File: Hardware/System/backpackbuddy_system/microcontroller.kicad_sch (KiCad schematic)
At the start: 10 parts, among them SW2 MCU RESET, U1 ATmega32U4-A, Y1 16MHz

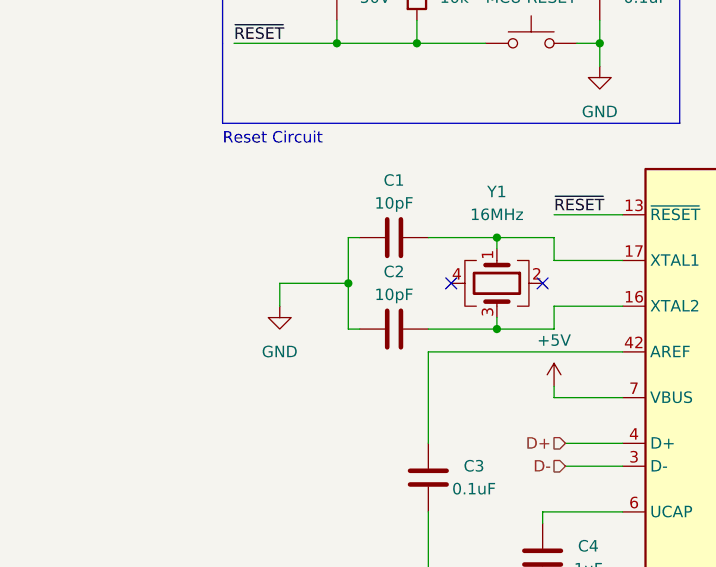
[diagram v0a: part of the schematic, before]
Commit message: fixed table values
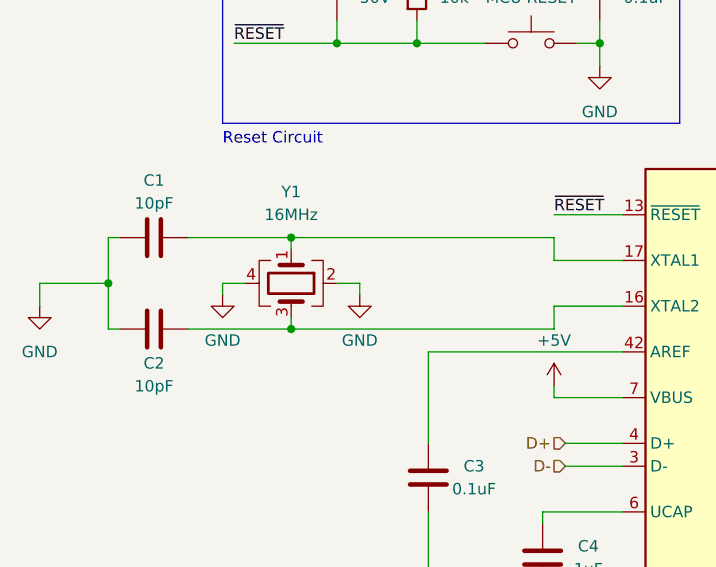
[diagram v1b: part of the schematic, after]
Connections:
- net GND: now also Y1.2, Y1.4
- no-connect marks 11 -> 9
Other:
- moved on the sheet: C1, C2, Y1

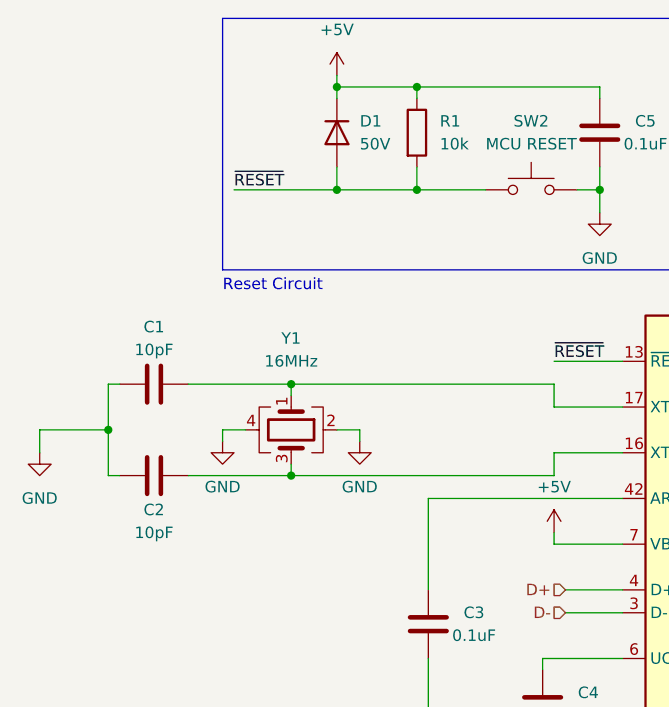
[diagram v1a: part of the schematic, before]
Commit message: changed D1, the MCU reset switch diode from 50V to 1V, changed crystal caps to 22pF
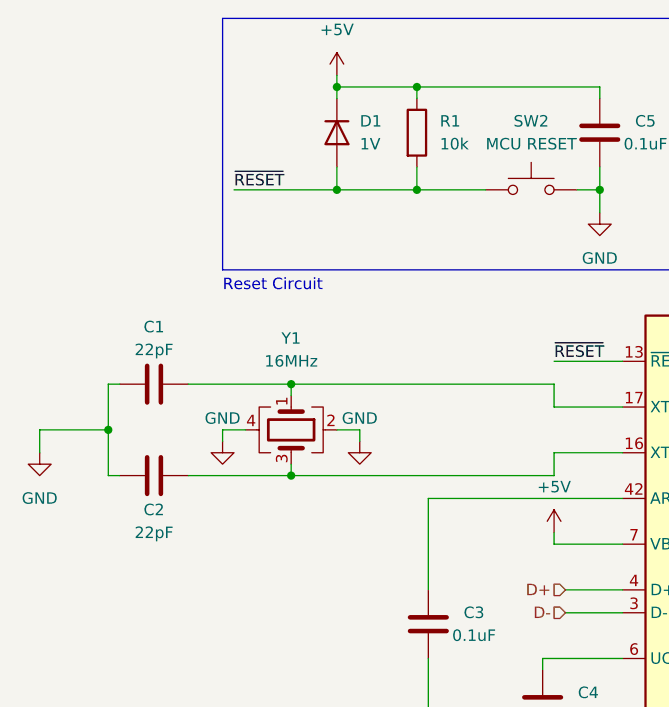
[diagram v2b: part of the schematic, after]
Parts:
- C1, C2: value 10pF -> 22pF
- D1: value 50V -> 1V; MPN DIODE SCHOTTKY 50V 1A SMB -> DIODE RECTIFIER 1V 2A SMB; Stock https://www.digikey.com/en/products/detail/diodes-incorpora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 -> https://www.digikey.com/en/products/detail/micro-commercial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
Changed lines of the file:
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@@
       (effects (font (size 1.27 1.27)) (justify left))
     )
-    (property "Value" "50V" (id 1) (at 102.87 46.9899 90)
+    (property "Value" "1V" (id 1) (at 102.87 46.9899 90)
       (effects (font (size 1.27 1.27)) (justify left))
     )
@@
       (effects (font (size 1.27 1.27)) hide)
     )
-    (property "Datasheet" "~" (id 3) (at 100.33 45.72 0)
-      (effects (font (size 1.27 1.27)) hide)
-    )
-    (property "MPN" "DIODE SCHOTTKY 50V 1A SMB" (id 4) (at 100.33 45.72 0)
-      (effects (font (size 1.27 1.27)) hide)
-    )
-    (property "Stock" "https://www.digikey.com/en/products/detail/diodes-incorporated/B150B-13-F/775856?utm_adgroup=General&utm_source=google&utm_medium=cpc&utm_campaign=PMax%20Shopping_Product_Zombie%20SKUs&utm_term=&utm_content=General" (id 5) (at 100.33 45.72 0)
+    (property "Datasheet" "https://www.mccsemi.com/pdf/Products/US2A-US2M(DO-214AA).pdf" (id 3) (at 100.33 45.72 0)
+      (effects (font (size 1.27 1.27)) hide)
+    )
+    (property "MPN" "DIODE RECTIFIER 1V 2A SMB" (id 4) (at 100.33 45.72 0)
+      (effects (font (size 1.27 1.27)) hide)
+    )
+    (property "Stock" "https://www.digikey.com/en/products/detail/micro-commercial-co/US2D-TP/4936172" (id 5) (at 100.33 45.72 0)
       (effects (font (size 1.27 1.27)) hide)
     )
@@
   )
   (symbol (lib_id "power:GND") (at 87.63 80.01 0) (unit 1)
-    (in_bom yes) (on_board yes) (fields_autoplaced)
+    (in_bom yes) (on_board yes)
     (property "Reference" "#PWR0108" (id 0) (at 87.63 86.36 0)
       (effects (font (size 1.27 1.27)) hide)
     )
-    (property "Value" "GND" (id 1) (at 87.63 85.09 0))
+    (property "Value" "GND" (id 1) (at 87.63 77.47 0))
     (property "Footprint" "" (id 2) (at 87.63 80.01 0)
       (effects (font (size 1.27 1.27)) hide)
@@
   )
   (symbol (lib_id "power:GND") (at 102.87 80.01 0) (unit 1)
-    (in_bom yes) (on_board yes) (fields_autoplaced)
+    (in_bom yes) (on_board yes)
     (property "Reference" "#PWR0107" (id 0) (at 102.87 86.36 0)
       (effects (font (size 1.27 1.27)) hide)
     )
-    (property "Value" "GND" (id 1) (at 102.87 85.09 0))
+    (property "Value" "GND" (id 1) (at 102.87 77.47 0))
     (property "Footprint" "" (id 2) (at 102.87 80.01 0)
       (effects (font (size 1.27 1.27)) hide)
@@
     (in_bom yes) (on_board yes)
     (property "Reference" "C2" (id 0) (at 80.01 87.63 90))
-    (property "Value" "10pF" (id 1) (at 80.01 90.17 90))
+    (property "Value" "22pF" (id 1) (at 80.01 90.17 90))
     (property "Footprint" "Capacitor_SMD:C_0805_2012Metric_Pad1.18x1.45mm_HandSolder" (id 2) (at 83.82 82.8548 0)
       (effects (font (size 1.27 1.27)) hide)
@@
     (in_bom yes) (on_board yes)
     (property "Reference" "C1" (id 0) (at 80.01 67.31 90))
-    (property "Value" "10pF" (id 1) (at 80.01 69.85 90))
+    (property "Value" "22pF" (id 1) (at 80.01 69.85 90))
     (property "Footprint" "Capacitor_SMD:C_0805_2012Metric_Pad1.18x1.45mm_HandSolder" (id 2) (at 83.82 72.6948 0)
       (effects (font (size 1.27 1.27)) hide)

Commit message: decoupling caps
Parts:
- added C20, C21, C22: 10uF, Capacitor_SMD:C_0805_2012Metric_Pad1.18x1.45mm_HandSolder, symbol Device:C
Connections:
- net +5V: now also C20.1, C21.1, C22.1
- net GND: now also C20.2, C21.2, C22.2
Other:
- note added: "MCU DECOUPLING CAPS"
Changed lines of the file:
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@@
   (junction (at 110.49 114.3) (diameter 0) (color 0 0 0 0)
   )
+  (junction (at 185.42 41.91) (diameter 0) (color 0 0 0 0)
+  )
   (junction (at 95.25 83.82) (diameter 0) (color 0 0 0 0)
   )
@@
   (junction (at 144.78 157.48) (diameter 0) (color 0 0 0 0)
   )
+  (junction (at 176.53 41.91) (diameter 0) (color 0 0 0 0)
+  )
+  (junction (at 176.53 54.61) (diameter 0) (color 0 0 0 0)
+  )
   (junction (at 74.93 78.74) (diameter 0) (color 0 0 0 0)
   )
@@
   )
   (junction (at 109.22 40.64) (diameter 0) (color 0 0 0 0)
+  )
+  (junction (at 185.42 54.61) (diameter 0) (color 0 0 0 0)
   )
   (junction (at 100.33 52.07) (diameter 0) (color 0 0 0 0)
@@
     (stroke (width 0) (type default) (color 0 0 0 0))
   )
+  (wire (pts (xy 176.53 52.07) (xy 176.53 54.61))
+    (stroke (width 0) (type default) (color 0 0 0 0))
+  )
   (wire (pts (xy 162.56 78.74) (xy 172.72 78.74))
     (stroke (width 0) (type default) (color 0 0 0 0))
@@
     (stroke (width 0) (type default) (color 0 0 0 0))
   )
+  (wire (pts (xy 185.42 54.61) (xy 194.31 54.61))
+    (stroke (width 0) (type default) (color 0 0 0 0))
+  )
   (wire (pts (xy 162.56 76.2) (xy 172.72 76.2))
     (stroke (width 0) (type default) (color 0 0 0 0))
@@
     (stroke (width 0) (type default) (color 0 0 0 0))
   )
+  (wire (pts (xy 185.42 41.91) (xy 185.42 44.45))
+    (stroke (width 0) (type default) (color 0 0 0 0))
+  )
   (wire (pts (xy 162.56 73.66) (xy 172.72 73.66))
     (stroke (width 0) (type default) (color 0 0 0 0))
@@
     (stroke (width 0) (type default) (color 0 0 0 0))
   )
+  (wire (pts (xy 176.53 41.91) (xy 176.53 44.45))
+    (stroke (width 0) (type default) (color 0 0 0 0))
+  )
   (wire (pts (xy 162.56 71.12) (xy 172.72 71.12))
     (stroke (width 0) (type default) (color 0 0 0 0))
@@
     (stroke (width 0) (type default) (color 0 0 0 0))
   )
+  (wire (pts (xy 176.53 54.61) (xy 185.42 54.61))
+    (stroke (width 0) (type default) (color 0 0 0 0))
+  )
   (wire (pts (xy 162.56 96.52) (xy 172.72 96.52))
     (stroke (width 0) (type default) (color 0 0 0 0))
@@
     (stroke (width 0) (type default) (color 0 0 0 0))
   )
+  (wire (pts (xy 185.42 41.91) (xy 194.31 41.91))
+    (stroke (width 0) (type default) (color 0 0 0 0))
+  )
   (wire (pts (xy 162.56 139.7) (xy 172.72 139.7))
     (stroke (width 0) (type default) (color 0 0 0 0))
@@
     (stroke (width 0) (type default) (color 0 0 0 0))
   )
+  (wire (pts (xy 185.42 52.07) (xy 185.42 54.61))
+    (stroke (width 0) (type default) (color 0 0 0 0))
+  )
+  (wire (pts (xy 194.31 44.45) (xy 194.31 41.91))
+    (stroke (width 0) (type default) (color 0 0 0 0))
+  )
   (polyline (pts (xy 138.43 60.96) (xy 87.63 60.96))
     (stroke (width 0) (type default) (color 0 0 0 0))
@@
     (stroke (width 0) (type default) (color 0 0 0 0))
   )
+  (wire (pts (xy 176.53 40.64) (xy 176.53 41.91))
+    (stroke (width 0) (type default) (color 0 0 0 0))
+  )
   (wire (pts (xy 162.56 104.14) (xy 172.72 104.14))
     (stroke (width 0) (type default) (color 0 0 0 0))
@@
     (stroke (width 0) (type default) (color 0 0 0 0))
   )
+  (wire (pts (xy 176.53 54.61) (xy 176.53 55.88))
+    (stroke (width 0) (type default) (color 0 0 0 0))
+  )
   (wire (pts (xy 125.73 96.52) (xy 132.08 96.52))
     (stroke (width 0) (type default) (color 0 0 0 0))
   )
+  (wire (pts (xy 194.31 52.07) (xy 194.31 54.61))
+    (stroke (width 0) (type default) (color 0 0 0 0))
+  )
   (wire (pts (xy 144.78 63.5) (xy 144.78 58.42))
     (stroke (width 0) (type default) (color 0 0 0 0))
@@
     (stroke (width 0) (type default) (color 0 0 0 0))
   )
+  (wire (pts (xy 176.53 41.91) (xy 185.42 41.91))
+    (stroke (width 0) (type default) (color 0 0 0 0))
+  )
   (wire (pts (xy 162.56 134.62) (xy 172.72 134.62))
     (stroke (width 0) (type default) (color 0 0 0 0))
+  )
+  (text "MCU DECOUPLING CAPS" (at 173.99 33.02 0)
+    (effects (font (size 1.27 1.27)) (justify left bottom))
   )
   (text "Reset Circuit" (at 87.63 63.5 0)
@@
   (hierarchical_label "PF6" (shape bidirectional) (at 172.72 142.24 0)
     (effects (font (size 1.27 1.27)) (justify left))
+  )
+  (symbol (lib_id "Device:C") (at 176.53 48.26 0) (unit 1)
+    (in_bom yes) (on_board yes)
+    (property "Reference" "C20" (id 0) (at 170.18 48.26 0)
+      (effects (font (size 1.27 1.27)) (justify left))
+    )
+    (property "Value" "10uF" (id 1) (at 170.18 50.8 0)
+      (effects (font (size 1.27 1.27)) (justify left))
+    )
+    (property "Footprint" "Capacitor_SMD:C_0805_2012Metric_Pad1.18x1.45mm_HandSolder" (id 2) (at 177.4952 52.07 0)
+      (effects (font (size 1.27 1.27)) hide)
+    )
+    (property "Datasheet" "~" (id 3) (at 176.53 48.26 0)
+      (effects (font (size 1.27 1.27)) hide)
+    )
+    (property "MPN" "CAP CER 10UF 25V X5R 0805" (id 4) (at 176.53 48.26 0)
+      (effects (font (size 1.27 1.27)) hide)
+    )
+    (property "Stock" "https://www.digikey.com/en/products/detail/kyocera-avx/08053D106KAT4A/12153448?utm_adgroup=Capacitors&utm_source=google&utm_medium=cpc&utm_campaign=Shopping_Supplier_AVX%20Corporation&utm_term=&utm_content=Capacitors" (id 5) (at 176.53 48.26 0)
+      (effects (font (size 1.27 1.27)) hide)
+    )
+    (pin "1")
+    (pin "2")
   )
   (symbol (lib_id "Device:D") (at 100.33 45.72 270) (unit 1)
@@
     (pin "2")
   )
+  (symbol (lib_id "power:GND") (at 176.53 55.88 0) (unit 1)
+    (in_bom yes) (on_board yes) (fields_autoplaced)
+    (property "Reference" "#PWR042" (id 0) (at 176.53 62.23 0)
+      (effects (font (size 1.27 1.27)) hide)
+    )
+    (property "Value" "GND" (id 1) (at 176.53 60.96 0))
+    (property "Footprint" "" (id 2) (at 176.53 55.88 0)
+      (effects (font (size 1.27 1.27)) hide)
+    )
+    (property "Datasheet" "" (id 3) (at 176.53 55.88 0)
+      (effects (font (size 1.27 1.27)) hide)
+    )
+    (pin "1")
+  )
   (symbol (lib_id "power:GND") (at 67.31 81.28 0) (unit 1)
     (in_bom yes) (on_board yes) (fields_autoplaced)
@@
     )
     (pin "1")
+  )
+  (symbol (lib_id "Device:C") (at 194.31 48.26 0) (unit 1)
+    (in_bom yes) (on_board yes)
+    (property "Reference" "C22" (id 0) (at 187.96 48.26 0)
+      (effects (font (size 1.27 1.27)) (justify left))
+    )
+    (property "Value" "10uF" (id 1) (at 187.96 50.8 0)
+      (effects (font (size 1.27 1.27)) (justify left))
+    )
+    (property "Footprint" "Capacitor_SMD:C_0805_2012Metric_Pad1.18x1.45mm_HandSolder" (id 2) (at 195.2752 52.07 0)
+      (effects (font (size 1.27 1.27)) hide)
+    )
+    (property "Datasheet" "~" (id 3) (at 194.31 48.26 0)
+      (effects (font (size 1.27 1.27)) hide)
+    )
+    (property "MPN" "CAP CER 10UF 25V X5R 0805" (id 4) (at 194.31 48.26 0)
+      (effects (font (size 1.27 1.27)) hide)
+    )
+    (property "Stock" "https://www.digikey.com/en/products/detail/kyocera-avx/08053D106KAT4A/12153448?utm_adgroup=Capacitors&utm_source=google&utm_medium=cpc&utm_campaign=Shopping_Supplier_AVX%20Corporation&utm_term=&utm_content=Capacitors" (id 5) (at 194.31 48.26 0)
+      (effects (font (size 1.27 1.27)) hide)
+    )
+    (pin "1")
+    (pin "2")
   )
   (symbol (lib_id "Device:C") (at 80.01 83.82 90) (unit 1)
@@
     (pin "2")
   )
+  (symbol (lib_id "Device:C") (at 185.42 48.26 0) (unit 1)
+    (in_bom yes) (on_board yes)
+    (property "Reference" "C21" (id 0) (at 179.07 48.26 0)
+      (effects (font (size 1.27 1.27)) (justify left))
+    )
+    (property "Value" "10uF" (id 1) (at 179.07 50.8 0)
+      (effects (font (size 1.27 1.27)) (justify left))
+    )
+    (property "Footprint" "Capacitor_SMD:C_0805_2012Metric_Pad1.18x1.45mm_HandSolder" (id 2) (at 186.3852 52.07 0)
+      (effects (font (size 1.27 1.27)) hide)
+    )
+    (property "Datasheet" "~" (id 3) (at 185.42 48.26 0)
+      (effects (font (size 1.27 1.27)) hide)
+    )
+    (property "MPN" "CAP CER 10UF 25V X5R 0805" (id 4) (at 185.42 48.26 0)
+      (effects (font (size 1.27 1.27)) hide)
+    )
+    (property "Stock" "https://www.digikey.com/en/products/detail/kyocera-avx/08053D106KAT4A/12153448?utm_adgroup=Capacitors&utm_source=google&utm_medium=cpc&utm_campaign=Shopping_Supplier_AVX%20Corporation&utm_term=&utm_content=Capacitors" (id 5) (at 185.42 48.26 0)
+      (effects (font (size 1.27 1.27)) hide)
+    )
+    (pin "1")
+    (pin "2")
+  )
   (symbol (lib_id "power:GND") (at 129.54 54.61 0) (unit 1)
     (in_bom yes) (on_board yes) (fields_autoplaced)
@@
     (pin "2")
   )
+  (symbol (lib_id "power:+5V") (at 176.53 40.64 0) (unit 1)
+    (in_bom yes) (on_board yes) (fields_autoplaced)
+    (property "Reference" "#PWR041" (id 0) (at 176.53 44.45 0)
+      (effects (font (size 1.27 1.27)) hide)
+    )
+    (property "Value" "+5V" (id 1) (at 176.53 35.56 0))
+    (property "Footprint" "" (id 2) (at 176.53 40.64 0)
+      (effects (font (size 1.27 1.27)) hide)
+    )
+    (property "Datasheet" "" (id 3) (at 176.53 40.64 0)
+      (effects (font (size 1.27 1.27)) hide)
+    )
+    (pin "1")
+  )
 )

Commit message: almost done
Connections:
- net PB7: now reaches U1.12 (PB7)
- net PD5: no longer names the net of U1.22 (PD5)
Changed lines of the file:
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@@
   )
   (no_connect (at 172.72 134.62))
-  (no_connect (at 172.72 88.9))
   (no_connect (at 172.72 144.78))
   (no_connect (at 172.72 124.46))
@@
   (no_connect (at 172.72 132.08))
   (no_connect (at 172.72 127))
+  (no_connect (at 172.72 114.3))
   (no_connect (at 172.72 137.16))
   (no_connect (at 172.72 96.52))
@@
     (effects (font (size 1.27 1.27)) (justify left))
   )
-  (hierarchical_label "PD5" (shape bidirectional) (at 172.72 114.3 0)
-    (effects (font (size 1.27 1.27)) (justify left))
-  )
   (hierarchical_label "PB0" (shape bidirectional) (at 172.72 71.12 0)
     (effects (font (size 1.27 1.27)) (justify left))
@@
     (effects (font (size 1.27 1.27)) (justify left))
   )
+  (hierarchical_label "PB7" (shape bidirectional) (at 172.72 88.9 0)
+    (effects (font (size 1.27 1.27)) (justify left))
+  )

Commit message: first draft done :))) still errors but thats because i was too lazy to do no connects as of rn
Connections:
- net PC6: now reaches U1.31 (PC6)
- net PC7: now reaches U1.32 (PC7)
- net PF7: now reaches U1.36 (PF7)
- no-connect marks 9 -> 6
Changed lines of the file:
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@@
   )
   (no_connect (at 172.72 134.62))
-  (no_connect (at 172.72 144.78))
   (no_connect (at 172.72 124.46))
-  (no_connect (at 172.72 93.98))
   (no_connect (at 172.72 132.08))
   (no_connect (at 172.72 127))
   (no_connect (at 172.72 114.3))
   (no_connect (at 172.72 137.16))
-  (no_connect (at 172.72 96.52))
   (wire (pts (xy 100.33 78.74) (xy 102.87 78.74))
     (stroke (width 0) (type default) (color 0 0 0 0))
@@
     (effects (font (size 1.27 1.27)) (justify right))
   )
+  (hierarchical_label "PC7" (shape bidirectional) (at 172.72 96.52 0)
+    (effects (font (size 1.27 1.27)) (justify left))
+  )
   (hierarchical_label "PB4" (shape bidirectional) (at 172.72 81.28 0)
     (effects (font (size 1.27 1.27)) (justify left))
@@
   )
   (hierarchical_label "PB2" (shape bidirectional) (at 172.72 76.2 0)
+    (effects (font (size 1.27 1.27)) (justify left))
+  )
+  (hierarchical_label "PC6" (shape bidirectional) (at 172.72 93.98 0)
     (effects (font (size 1.27 1.27)) (justify left))
   )
@@
   (hierarchical_label "D+" (shape input) (at 125.73 96.52 180)
     (effects (font (size 1.27 1.27)) (justify right))
+  )
+  (hierarchical_label "PF7" (shape bidirectional) (at 172.72 144.78 0)
+    (effects (font (size 1.27 1.27)) (justify left))
   )
   (hierarchical_label "PD3{slash}TX" (shape bidirectional) (at 172.72 109.22 0)
@@
     (pin "2")
   )
-  (symbol (lib_id "power:GND") (at 144.78 160.02 0) (unit 1)
+  (symbol (lib_name "GND_6") (lib_id "power:GND") (at 144.78 160.02 0) (unit 1)
     (in_bom yes) (on_board yes) (fields_autoplaced)
     (property "Reference" "#PWR025" (id 0) (at 144.78 166.37 0)
@@
     (pin "4")
   )
-  (symbol (lib_id "power:GND") (at 87.63 80.01 0) (unit 1)
+  (symbol (lib_name "GND_3") (lib_id "power:GND") (at 87.63 80.01 0) (unit 1)
     (in_bom yes) (on_board yes)
     (property "Reference" "#PWR0108" (id 0) (at 87.63 86.36 0)
@@
     (pin "1")
   )
-  (symbol (lib_id "power:GND") (at 102.87 80.01 0) (unit 1)
+  (symbol (lib_name "GND_4") (lib_id "power:GND") (at 102.87 80.01 0) (unit 1)
     (in_bom yes) (on_board yes)
     (property "Reference" "#PWR0107" (id 0) (at 102.87 86.36 0)
@@
     (pin "1")
   )
-  (symbol (lib_id "power:GND") (at 110.49 115.57 0) (unit 1)
+  (symbol (lib_name "GND_1") (lib_id "power:GND") (at 110.49 115.57 0) (unit 1)
     (in_bom yes) (on_board yes) (fields_autoplaced)
     (property "Reference" "#PWR021" (id 0) (at 110.49 121.92 0)
@@
     (pin "1")
   )
-  (symbol (lib_id "power:GND") (at 67.31 81.28 0) (unit 1)
+  (symbol (lib_name "GND_5") (lib_id "power:GND") (at 67.31 81.28 0) (unit 1)
     (in_bom yes) (on_board yes) (fields_autoplaced)
     (property "Reference" "#PWR019" (id 0) (at 67.31 87.63 0)
@@
     (pin "2")
   )
-  (symbol (lib_id "power:GND") (at 129.54 54.61 0) (unit 1)
+  (symbol (lib_name "GND_2") (lib_id "power:GND") (at 129.54 54.61 0) (unit 1)
     (in_bom yes) (on_board yes) (fields_autoplaced)
     (property "Reference" "#PWR023" (id 0) (at 129.54 60.96 0)

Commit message: Board run 2 start -> rewire arduino connections
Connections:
- net PD0 renamed PD0/SCL
- net PD1 renamed PD1/SDA
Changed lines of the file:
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@@
     (effects (font (size 1.27 1.27)) (justify left bottom))
   )
-  (hierarchical_label "PD1" (shape bidirectional) (at 172.72 104.14 0)
+  (hierarchical_label "PD1{slash}SDA" (shape bidirectional) (at 172.72 104.14 0)
     (effects (font (size 1.27 1.27)) (justify left))
   )
@@
     (effects (font (size 1.27 1.27)) (justify left))
   )
-  (hierarchical_label "PD0" (shape bidirectional) (at 172.72 101.6 0)
+  (hierarchical_label "PD0{slash}SCL" (shape bidirectional) (at 172.72 101.6 0)
     (effects (font (size 1.27 1.27)) (justify left))
   )

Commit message: version 3 board
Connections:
- net PB1 renamed PB1/SCLK
- net PB2 renamed PB2/MOSI
- net PB3 renamed PB3/MISO
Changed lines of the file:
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@@
     (effects (font (size 1.27 1.27)) (justify left))
   )
-  (hierarchical_label "PB2" (shape bidirectional) (at 172.72 76.2 0)
+  (hierarchical_label "PB2{slash}MOSI" (shape bidirectional) (at 172.72 76.2 0)
     (effects (font (size 1.27 1.27)) (justify left))
   )
@@
     (effects (font (size 1.27 1.27)) (justify left))
   )
-  (hierarchical_label "PB1" (shape bidirectional) (at 172.72 73.66 0)
+  (hierarchical_label "PB1{slash}SCLK" (shape bidirectional) (at 172.72 73.66 0)
     (effects (font (size 1.27 1.27)) (justify left))
   )
@@
     (effects (font (size 1.27 1.27)) (justify left))
   )
-  (hierarchical_label "PB3" (shape bidirectional) (at 172.72 78.74 0)
+  (hierarchical_label "PB3{slash}MISO" (shape bidirectional) (at 172.72 78.74 0)
     (effects (font (size 1.27 1.27)) (justify left))
   )
@@
     (effects (font (size 1.27 1.27)) (justify left))
   )
+  (hierarchical_label "~{RESET}" (shape bidirectional) (at 124.46 71.12 180)
+    (effects (font (size 1.27 1.27)) (justify right))
+  )
   (hierarchical_label "PB7" (shape bidirectional) (at 172.72 88.9 0)
